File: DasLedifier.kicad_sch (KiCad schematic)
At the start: 14 parts, among them J1 USB_C_Receptacle, J3 MCU_DEBUG, SW1 RESET_BUTTON, U1 STUSB4500QTR, U4 STM32F070CBTx, U5 MRF24J40MA-I/RM, U6 TPS56837HRPAR

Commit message: Last commit of v1
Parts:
- added C14: 22nF, Capacitor_SMD:C_0805_2012Metric, symbol Device:C_Small
- added C15: 0.1uF, Capacitor_SMD:C_0805_2012Metric, symbol Device:C_Small
- added C16, C17: 10uF, Capacitor_SMD:C_0805_2012Metric, symbol Device:C_Small
- added R11: 30.1k, Resistor_SMD:R_0805_2012Metric, symbol Device:R_Small
- added R12: 36.1k, Resistor_SMD:R_0805_2012Metric, symbol Device:R_Small
- added R13: 169k, Resistor_SMD:R_0805_2012Metric, symbol Device:R_Small
- added R19: 0k, symbol Device:R_Small
- added SW2: SW_Nidec_CAS-120A1, Button_Switch_SMD:Nidec_Copal_CAS-120A, symbol Switch:SW_Nidec_CAS-120A1
- D6, D8: footprint (none) -> LED_SMD:LED_0805_2012Metric
- J1: footprint Connector_USB:USB_C_Receptacle_Amphenol_12401548E4-2A -> Connector_USB:USB_C_Receptacle_G-Switch_GT-USB-7010ASV
- R10, R9: footprint (none) -> Resistor_SMD:R_0805_2012Metric
- U6: footprint RPA0010A-MFG -> STUSB4500QTR:RPA0010A-MFG
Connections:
- net +3V3: now also SW2.3 (A)
- net DISCH: now also R6.1, U1.9 (DISCH); no longer R6.2
- net GND: now also U6.9 (PGND), C15.2, C16.2, C17.2, R11.1, R12.1, R19.2, SW2.1 (C); no longer U5.1 (GND), U5.11 (GND), U5.12 (GND)
- net MCU_BOOT_SELECT: now also SW2.2 (B)
- net VDD: now also R6.2, U6.8 (VIN), C15.1, C16.1, C17.1, R13.1
- net at U6.1 (EN): now also R12.2, R13.2
- net at U6.10 (MODE): now also R11.2
- net BB_FB: now reaches U6.2 (FB)
- net BB_AGND: now reaches U6.3 (AGND)
- net BB_AGND: now also C14.2, R19.1
- net BB_PG: now reaches U6.4 (PG)
- net at U6.5 (SS): now also C14.1
- net BB_SW: now reaches U6.6 (SW)
- net BB_BOOT: now reaches U6.7 (BOOT)
- no-connect marks 47 -> 50
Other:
- added sheet 5V_POWER (5V_POWER.kicad_sch)
- note added: "9.6A current limit"
- note added: "min soft-startup (2.2ms)"
- moved on the sheet: C13, D6, D8, J3, R10, R9, SW1, U6

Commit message: Progress
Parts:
- removed C13, C15: 0.1uF, Capacitor_SMD:C_0805_2012Metric, symbol Device:C_Small
- removed C14: 22nF, Capacitor_SMD:C_0805_2012Metric, symbol Device:C_Small
- removed C16, C17: 10uF, Capacitor_SMD:C_0805_2012Metric, symbol Device:C_Small
- removed D6: PWR_LED, LED_SMD:LED_0805_2012Metric, symbol Device:LED
- removed D8: PD_SUCCESS, LED_SMD:LED_0805_2012Metric, symbol Device:LED
- removed J1: USB_C_Receptacle, Connector_USB:USB_C_Receptacle_G-Switch_GT-USB-7010ASV, symbol Connector:USB_C_Receptacle
- removed J3: MCU_DEBUG, Connector:Tag-Connect_TC2030-IDC-NL_2x03_P1.27mm_Vertical, symbol Connector:Conn_ARM_SWD_TagConnect_TC2030-NL
- removed R10, R9: LED Value, Resistor_SMD:R_0805_2012Metric, symbol Device:R_Small
- removed R11: 30.1k, Resistor_SMD:R_0805_2012Metric, symbol Device:R_Small
- removed R12: 36.1k, Resistor_SMD:R_0805_2012Metric, symbol Device:R_Small
- removed R13: 169k, Resistor_SMD:R_0805_2012Metric, symbol Device:R_Small
- removed R19: 0k, symbol Device:R_Small
- removed R6: 1k, Resistor_SMD:R_0805_2012Metric, symbol Device:R_Small
- removed SW1: RESET_BUTTON, Button_Switch_THT:SW_PUSH_6mm, symbol Switch:SW_Push
- removed SW2: SW_Nidec_CAS-120A1, Button_Switch_SMD:Nidec_Copal_CAS-120A, symbol Switch:SW_Nidec_CAS-120A1
- removed U1: STUSB4500QTR, Package_DFN_QFN:QFN-24-1EP_4x4mm_P0.5mm_EP2.7x2.7mm, symbol Interface_USB:STUSB4500QTR
- removed U4: STM32F070CBTx, Package_QFP:LQFP-48_7x7mm_P0.5mm, symbol MCU_ST_STM32F0:STM32F070CBTx
- removed U5: MRF24J40MA-I/RM, STUSB4500QTR:MOD12_MRF24J40MA_MCH, symbol MRF:MRF24J40MA-I_RM
- removed U6: TPS56837HRPAR, STUSB4500QTR:RPA0010A-MFG, symbol aa:TPS56837HRPAR
- added U1: PTPS55289RYQR, footprints:RYQ0021A-MFG, symbol 2024-02-28_02-41-41:PTPS55289RYQR
- added U2: STUSB4500QTR, Package_DFN_QFN:QFN-24-1EP_4x4mm_P0.5mm_EP2.7x2.7mm, symbol Interface_USB:STUSB4500QTR
- added U3: STM32F070CBTx, Package_QFP:LQFP-48_7x7mm_P0.5mm, symbol MCU_ST_STM32F0:STM32F070CBTx
- added U4: CC2520, Package_DFN_QFN:QFN-28-1EP_5x5mm_P0.5mm_EP3.35x3.35mm, symbol RF_ZigBee:CC2520
- R7: value 4.7k -> R_Small
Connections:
- net GND: now also U2.22 (VSYS); no longer R7.2
- net VDD: now also R7.1, U2.24 (VDD)
- new net: R7.2, U1.1 (EN_UVLO), U1.2 (MODE)
- new net: U3.23 (VSS), U3.35 (VSS), U3.47 (VSS)
- new net: U2.10 (GND), U2.25 (GND)
- new net BB_SCL: U1.3 (SCL)
- new net BB_SDA: U1.4 (SDA)
- new net LED_SUPPLY/AGND: U1.17 (AGND)
- new net LED_SUPPLY/BOOT1: U1.20 (BOOT1)
- new net LED_SUPPLY/BOOT2: U1.19 (BOOT2)
- new net LED_SUPPLY/CDC: U1.16 (CDC)
- new net LED_SUPPLY/COMP: U1.15 (COMP)
- new net LED_SUPPLY/FSW: U1.6 (FSW)
- new net LED_SUPPLY/ISN: U1.13 (ISN)
- new net LED_SUPPLY/ISP: U1.12 (ISP)
- new net LED_SUPPLY/PGND: U1.9 (PGND)
- new net LED_SUPPLY/SW1: U1.8 (SW1)
- new net LED_SUPPLY/SW2: U1.10 (SW2)
- new net LED_SUPPLY/SYNC: U1.5 (DITH_SYNC)
- new net LED_SUPPLY/VOUT: U1.11 (VOUT)
- new net PD_VBUS: U1.7 (VIN)
- new net VCC: U1.18 (VCC)
- no-connect marks 50 -> 23
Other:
- removed sheet 5V_POWER
- removed sheet MCU
- removed sheet USB_C_PORT_POWER
- added sheet LED_SUPPLY (LED_SUPPLY.kicad_sch)
- added sheet PD_CONTROLLER (PD_CONTROLLER.kicad_sch)
- note added: "Set IC2 Addr"
- note added: "use internal vcc"
- note removed: "9.6A current limit"
- note removed: "min soft-startup (2.2ms)"
- note removed: "unclear whether I need wake\"
- title: DasLedifier -> (none)

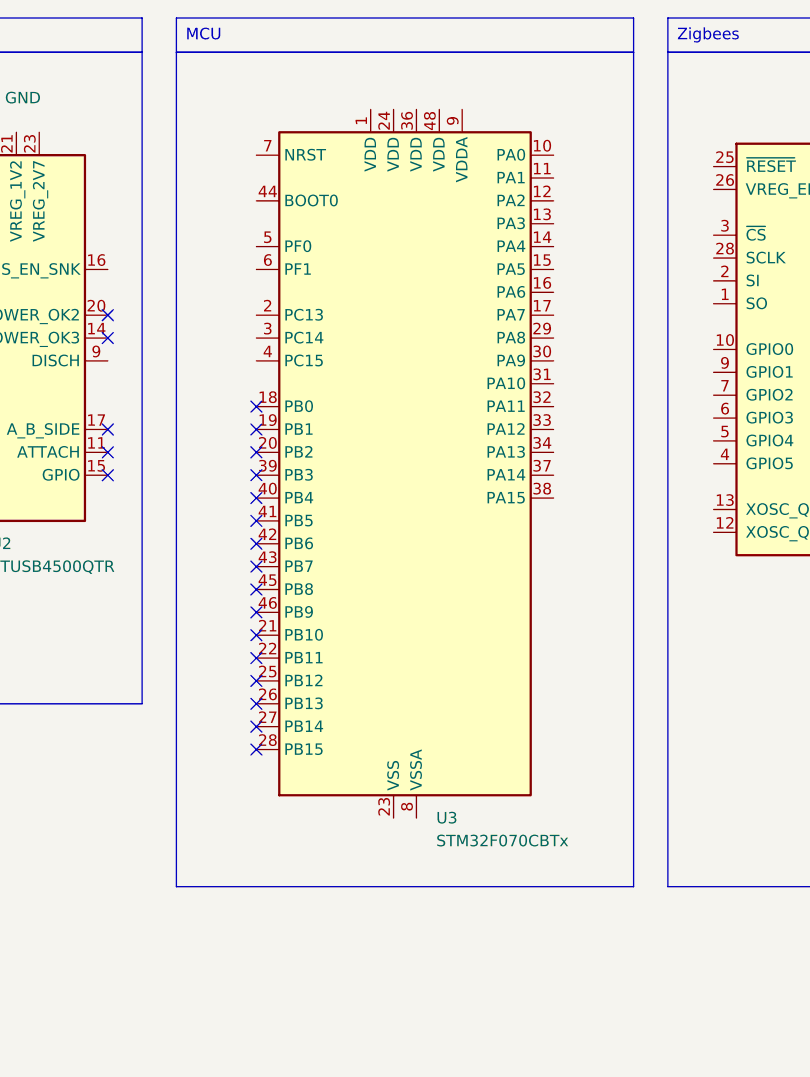
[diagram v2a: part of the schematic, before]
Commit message: Basic STM32 hook-up and reference
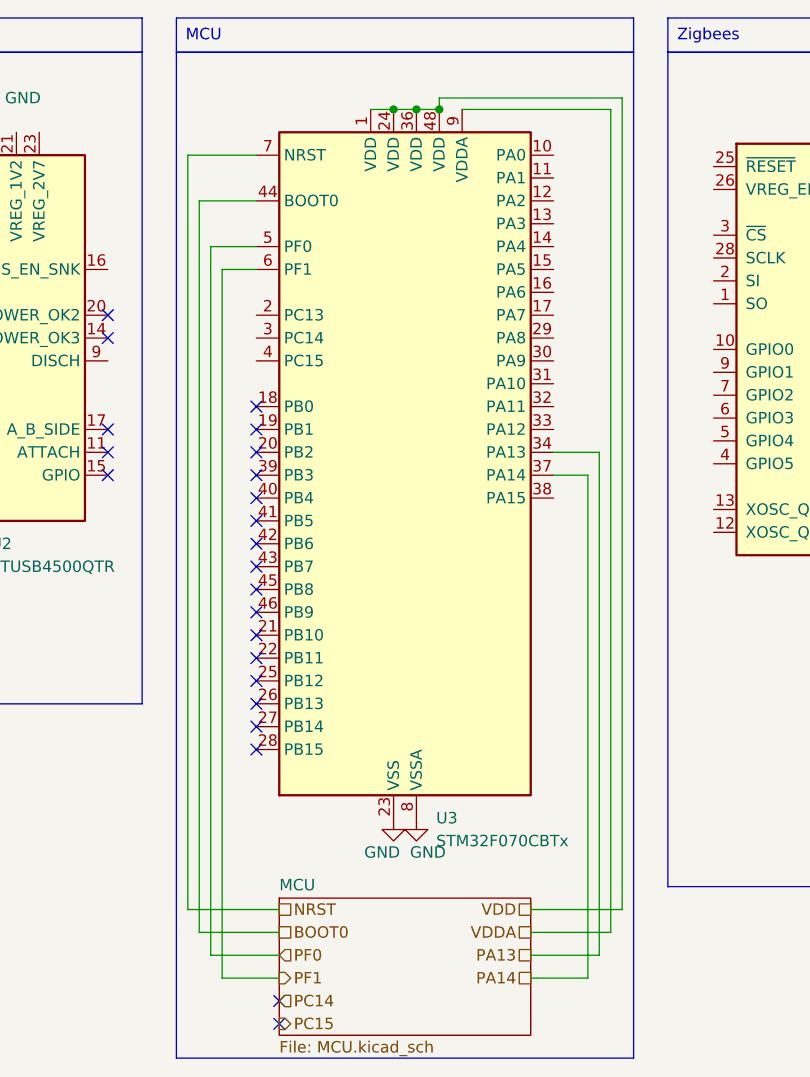
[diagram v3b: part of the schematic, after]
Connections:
- net GND: now also U3.23 (VSS), U3.35 (VSS), U3.47 (VSS), U3.8 (VSSA)
- net VDD: now also U3.1 (VDD), U3.24 (VDD), U3.36 (VDD), U3.48 (VDD)
- net PA13: now reaches U3.34 (PA13)
- net PA14: now reaches U3.37 (PA14)
- net BOOT0: now reaches U3.44 (BOOT0)
- net PF0: now reaches U3.5 (PF0)
- net PF1: now reaches U3.6 (PF1)
- net NRST: now reaches U3.7 (NRST)
- net VDDA: now reaches U3.9 (VDDA)
- no-connect marks 23 -> 25
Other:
- added sheet MCU (MCU.kicad_sch)

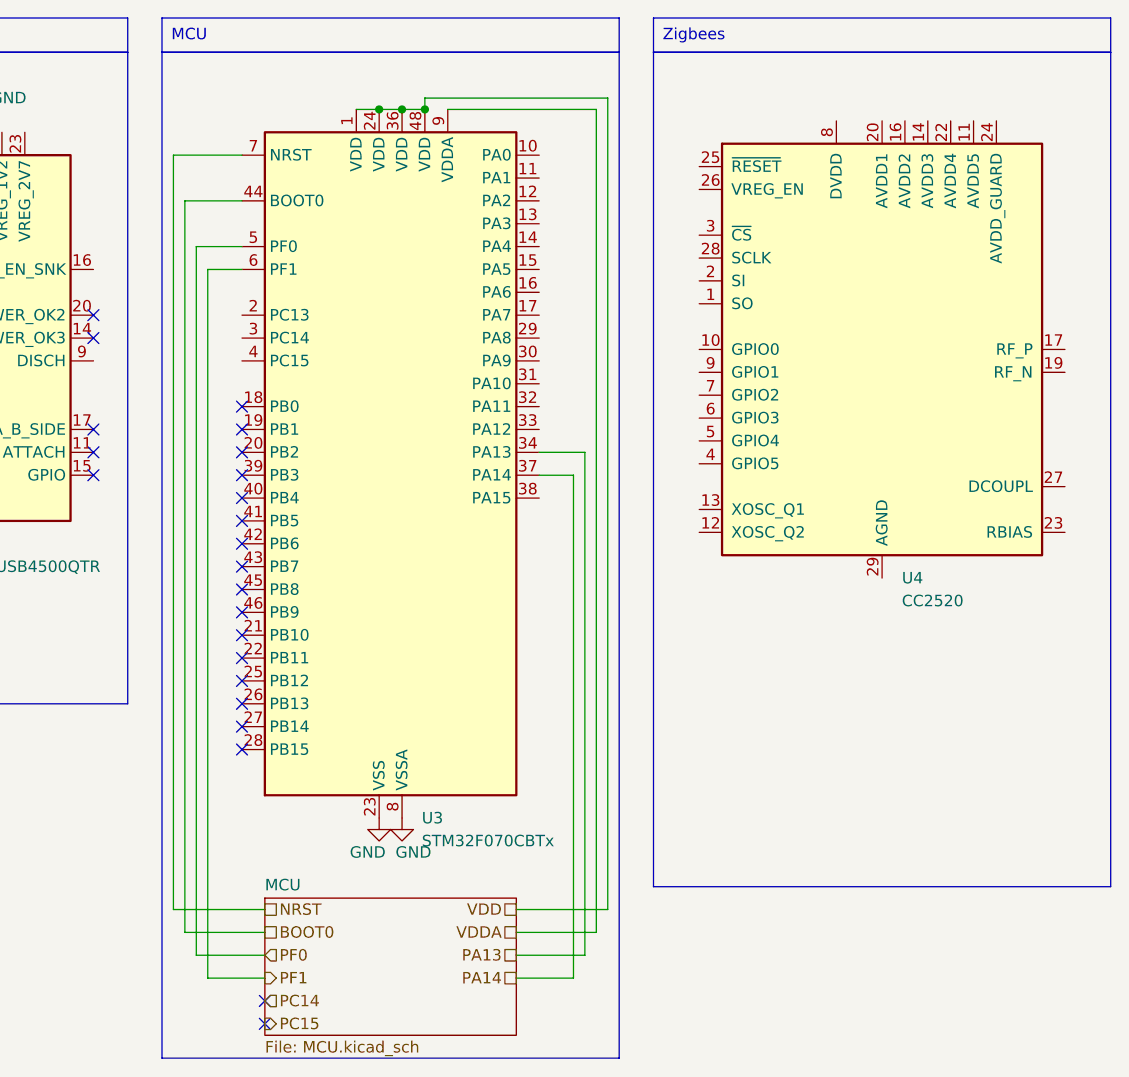
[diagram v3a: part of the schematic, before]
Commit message: Switch to new chip
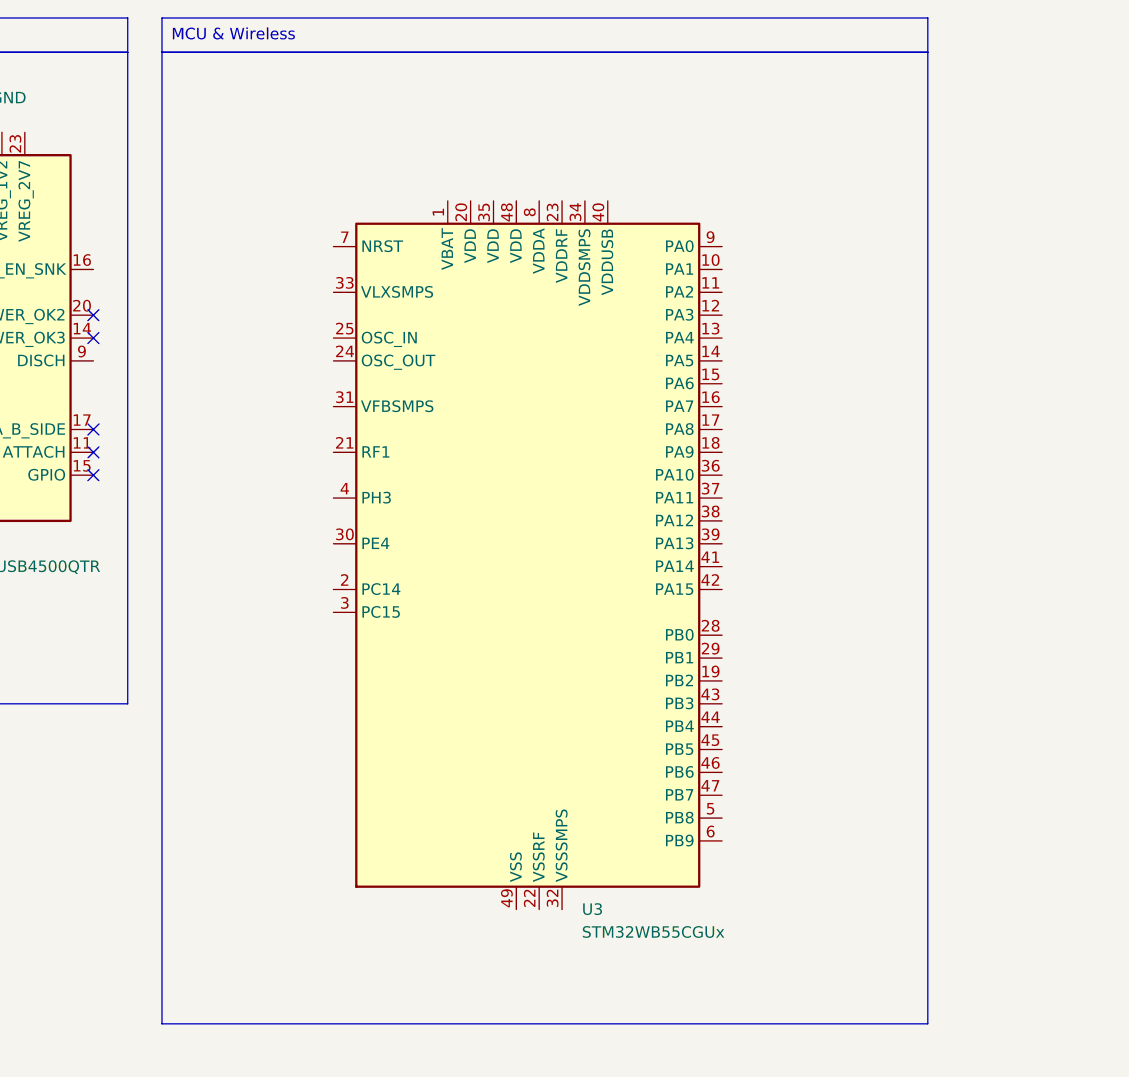
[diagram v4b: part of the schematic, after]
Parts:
- removed U3: STM32F070CBTx, Package_QFP:LQFP-48_7x7mm_P0.5mm, symbol MCU_ST_STM32F0:STM32F070CBTx
- removed U4: CC2520, Package_DFN_QFN:QFN-28-1EP_5x5mm_P0.5mm_EP3.35x3.35mm, symbol RF_ZigBee:CC2520
- added U3: STM32WB55CGUx, Package_DFN_QFN:QFN-48-1EP_7x7mm_P0.5mm_EP5.6x5.6mm, symbol MCU_ST_STM32WB:STM32WB55CGUx
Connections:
- no-connect marks 25 -> 7
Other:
- removed sheet MCU

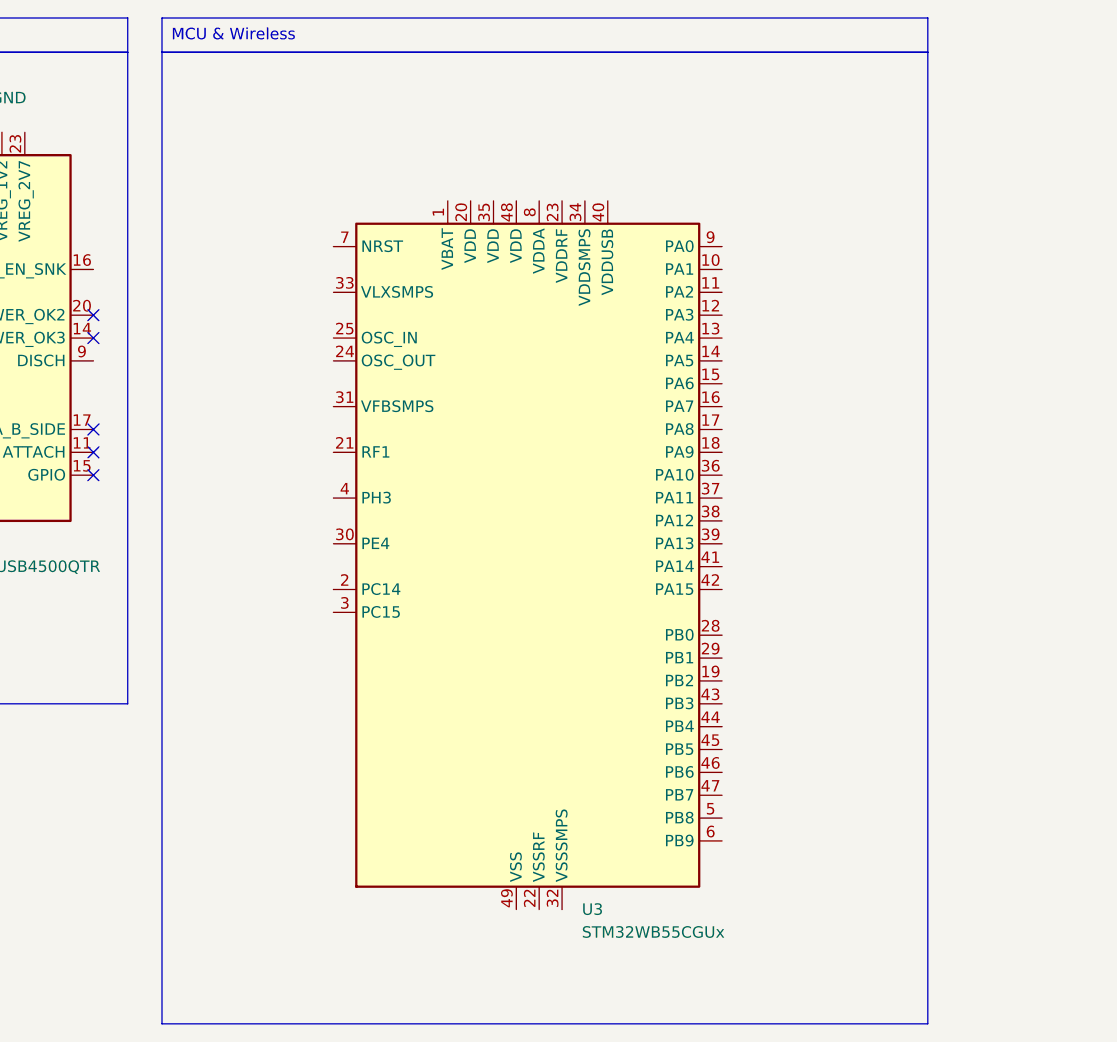
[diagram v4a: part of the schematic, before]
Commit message: Haven't checked LSE, NRST, BOOT0 and SWD
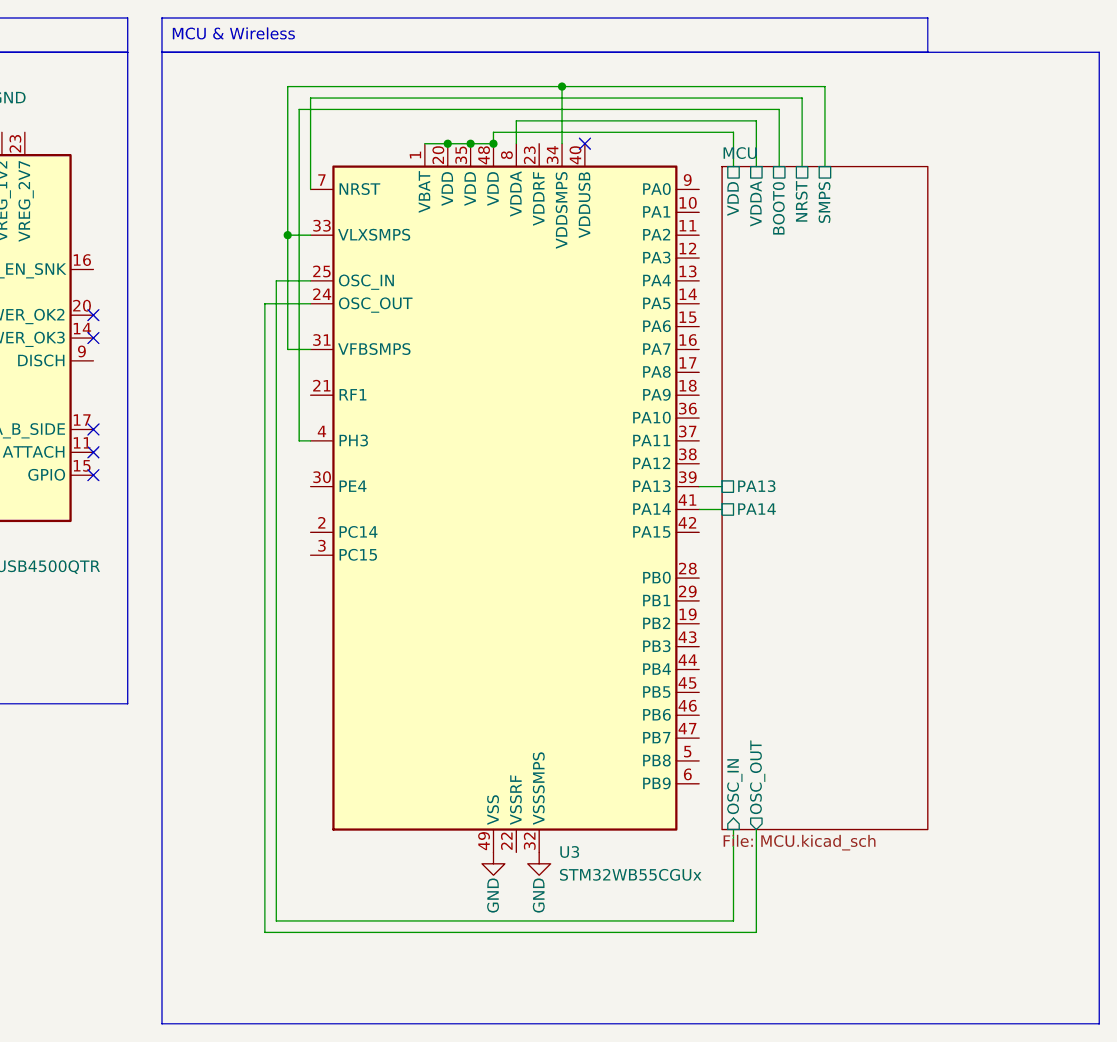
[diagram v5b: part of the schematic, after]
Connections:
- net GND: now also U3.32 (VSSSMPS), U3.49 (VSS)
- net MCU/VDD: now reaches U3.1 (VBAT)
- net MCU/VDD: now also U3.20 (VDD), U3.35 (VDD), U3.48 (VDD)
- net MCU/OSC_OUT: now reaches U3.24 (OSC_OUT)
- net MCU/OSC_IN: now reaches U3.25 (OSC_IN)
- net MCU/SMPS: now reaches U3.31 (VFBSMPS)
- net MCU/SMPS: now also U3.33 (VLXSMPS), U3.34 (VDDSMPS)
- net MCU/PA13: now reaches U3.39 (PA13)
- net MCU/BOOT0: now reaches U3.4 (PH3)
- net MCU/PA14: now reaches U3.41 (PA14)
- net MCU/NRST: now reaches U3.7 (NRST)
- net MCU/VDDA: now reaches U3.8 (VDDA)
- no-connect marks 7 -> 8
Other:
- added sheet MCU (MCU.kicad_sch)
- moved on the sheet: U3
